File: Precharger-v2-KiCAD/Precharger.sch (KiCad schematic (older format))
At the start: 61 parts, among them J1 Screw_Terminal_01x04, J2 Anderson_PP45_Power_RA, J3 Anderson_PP45_Power_RA, J5 Anderson_PP45_Power_RA, M1 Anderson_PP45_Staple_Nx2, M2 Anderson_PP45_Staple_Nx2, M3 Anderson_PP45_Staple_Nx2, Q1 SQJQ480E, Q2 BSS123, U1 MCP6001-OT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

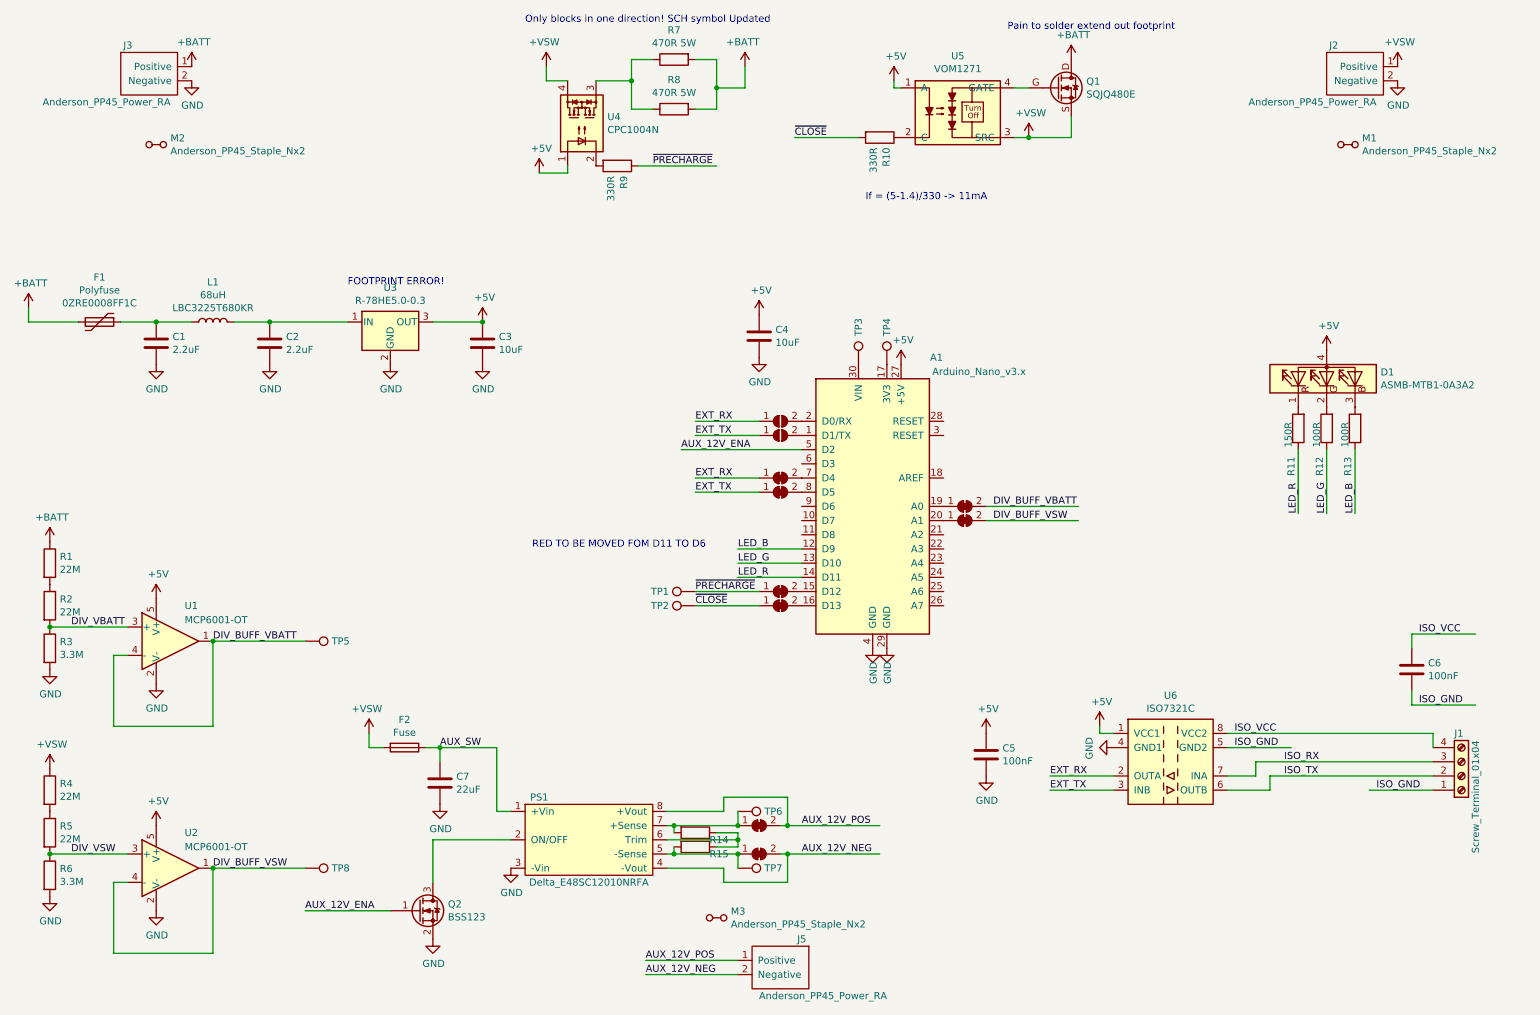
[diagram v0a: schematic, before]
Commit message: Getting a v2 going to try a buck precharge stage
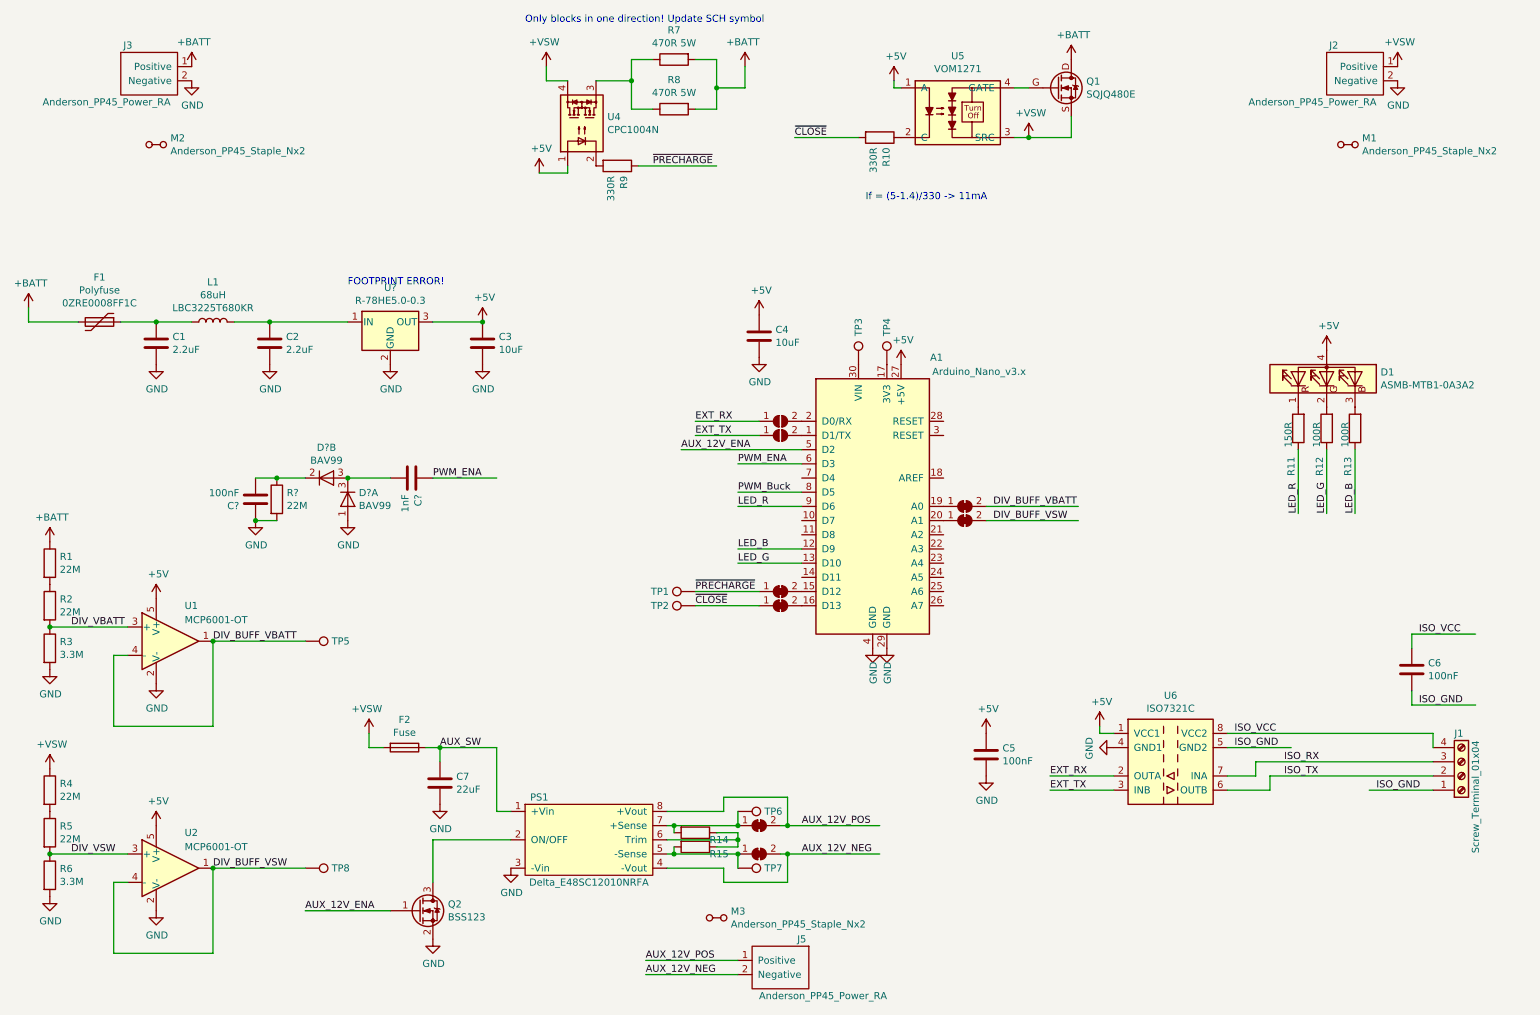
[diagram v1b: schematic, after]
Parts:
- removed JP3, JP4: SolderJumper_2_Bridged, Jumper:SolderJumper-2_P1.3mm_Bridged2Bar_RoundedPad1.0x1.5mm, symbol Jumper:SolderJumper_2_Bridged
- removed U3: R-78HE5.0-0.3, Converter_DCDC:Converter_DCDC_RECOM_R-78HB-0.5_THT, symbol Regulator_Switching:R-78HB5.0-0.5
- added C?: 1nF, Capacitor_SMD:C_0805_2012Metric_Pad1.15x1.40mm_HandSolder, symbol Device:C
- added C?: 100nF, Capacitor_SMD:C_0805_2012Metric_Pad1.15x1.40mm_HandSolder, symbol Device:C
- added D? (x2): BAV99, Package_TO_SOT_SMD:SOT-23, symbol Diode:BAV99
- added R?: 22M, Resistor_SMD:R_0805_2012Metric_Pad1.15x1.40mm_HandSolder, symbol Device:R
- added U?: R-78HE5.0-0.3, General_Library:Converter_DCDC_RECOM_R-78HE-0.3, symbol General_Library:R-78HE5.0-0.3
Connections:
- net labels added: PWM_Buck, PWM_ENA
- wire segments 112 -> 117
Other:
- note added: "Only blocks in one direction! Update SCH symbol"
- note removed: "Only blocks in one direction! SCH symbol Updated"
- note removed: "Pain to solder extend out footprint"
- note removed: "RED TO BE MOVED FOM D11 TO D6"
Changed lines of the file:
@@
-$EndComp
-$Comp
-L Regulator_Switching:R-78HB5.0-0.5 U3
-U 1 1 5DE55D69
-P 3400 2950
-F 0 "U3" H 3400 3192 50  0000 C CNN
-F 1 "R-78HE5.0-0.3" H 3400 3101 50  0000 C CNN
-F 2 "Converter_DCDC:Converter_DCDC_RECOM_R-78HB-0.5_THT" H 3450 2700 50  0001 L CIN
-F 3 "https://www.recom-power.com/pdf/Innoline/R-78HBxx-0.5_L.pdf" H 3400 2950 50  0001 C CNN
-	1    3400 2950
-	1    0    0    -1
 $EndComp
 $Comp
@@
 	1    0    0    -1
 $EndComp
-Text Label 5550 4150 0    50   ~ 0
-EXT_TX
-Text Label 5550 4050 0    50   ~ 0
-EXT_RX
-Wire Wire Line
-	6000 4150 5550 4150
-Wire Wire Line
-	6000 4050 5550 4050
 Text Label 5550 3750 0    50   ~ 0
 EXT_TX
@@
 Wire Wire Line
 	6000 3650 5550 3650
-$Comp
-L Jumper:SolderJumper_2_Bridged JP4
-U 1 1 5DE8F8F2
-P 6150 4150
-F 0 "JP4" H 6150 4263 50  0001 C CNN
-F 1 "SolderJumper_2_Bridged" H 6150 4264 50  0001 C CNN
-F 2 "Jumper:SolderJumper-2_P1.3mm_Bridged2Bar_RoundedPad1.0x1.5mm" H 6150 4150 50  0001 C CNN
-F 3 "~" H 6150 4150 50  0001 C CNN
-	1    6150 4150
-	1    0    0    -1
-$EndComp
 $Comp
 L power:GND #PWR0129
@@
 Wire Wire Line
 	6300 4550 5850 4550
+Text Label 5850 4250 0    50   ~ 0
+LED_R
 Wire Wire Line
 	6300 4650 5850 4650
 Text Label 5850 4650 0    50   ~ 0
 LED_G
+Wire Wire Line
+	6300 4250 5850 4250
 Text Label 5850 4550 0    50   ~ 0
 LED_B
@@
 FOOTPRINT ERROR!
 Text Notes 4350 850  0    50   ~ 0
-Only blocks in one direction! SCH symbol Updated
-Text Notes 7750 900  0    50   ~ 0
-Pain to solder extend out footprint
-$Comp
-L Jumper:SolderJumper_2_Bridged JP3
-U 1 1 5DE8EB88
-P 6150 4050
-F 0 "JP3" H 6150 4163 50  0001 C CNN
-F 1 "SolderJumper_2_Bridged" H 6150 4164 50  0001 C CNN
-F 2 "Jumper:SolderJumper-2_P1.3mm_Bridged2Bar_RoundedPad1.0x1.5mm" H 6150 4050 50  0001 C CNN
-F 3 "~" H 6150 4050 50  0001 C CNN
-	1    6150 4050
-	1    0    0    -1
-$EndComp
-Text Notes 4400 4550 0    50   ~ 0
-RED TO BE MOVED FOM D11 TO D6
-Wire Wire Line
-	6300 4750 5850 4750
-Text Label 5850 4750 0    50   ~ 0
-LED_R
+Only blocks in one direction! Update SCH symbol
+Text Label 5850 3950 0    50   ~ 0
+PWM_ENA
+Wire Wire Line
+	6300 3950 5850 3950
+Text Label 5850 4150 0    50   ~ 0
+PWM_Buck
+Wire Wire Line
+	6300 4150 5850 4150
+$Comp
+L Diode:BAV99 D?
+U 1 1 5E066B6B
+P 3100 4200
+F 0 "D?" V 3054 4278 50  0000 L CNN
+F 1 "BAV99" V 3145 4278 50  0000 L CNN
+F 2 "Package_TO_SOT_SMD:SOT-23" H 3100 4050 50  0001 C CNN
+F 3 "https://assets.nexperia.com/documents/data-sheet/BAV99_SER.pdf" H 3100 4300 50  0001 C CNN
+	1    3100 4200
+	0    1    1    0
+$EndComp
+$Comp
+L Diode:BAV99 D?
+U 2 1 5E068523
+P 2950 4050
+F 0 "D?" H 2950 4265 50  0000 C CNN
+F 1 "BAV99" H 2950 4174 50  0000 C CNN
+F 2 "Package_TO_SOT_SMD:SOT-23" H 2950 3900 50  0001 C CNN
+F 3 "https://assets.nexperia.com/documents/data-sheet/BAV99_SER.pdf" H 2950 4150 50  0001 C CNN
+	2    2950 4050
+	1    0    0    -1
+$EndComp
+$Comp
+L Device:C C?
+U 1 1 5E06EAA7
+P 3550 4050
+F 0 "C?" H 3665 4096 50  0000 L CNN
+F 1 "1nF" H 3665 4005 50  0000 L CNN
+F 2 "Capacitor_SMD:C_0805_2012Metric_Pad1.15x1.40mm_HandSolder" H 3588 3900 50  0001 C CNN
+F 3 "~" H 3550 4050 50  0001 C CNN
+	1    3550 4050
+	0    1    1    0
+$EndComp
+$Comp
+L power:GND #PWR?
+U 1 1 5E07408A
+P 3100 4350
+F 0 "#PWR?" H 3100 4100 50  0001 C CNN
+F 1 "GND" H 3105 4177 50  0000 C CNN
+F 2 "" H 3100 4350 50  0001 C CNN
+F 3 "" H 3100 4350 50  0001 C CNN
+	1    3100 4350
+	1    0    0    -1
+$EndComp
+$Comp
+L Device:C C?
+U 1 1 5E077AE9
+P 2450 4200
+F 0 "C?" H 2565 4246 50  0000 L CNN
+F 1 "100nF" H 2565 4155 50  0000 L CNN
+F 2 "Capacitor_SMD:C_0805_2012Metric_Pad1.15x1.40mm_HandSolder" H 2488 4050 50  0001 C CNN
+F 3 "~" H 2450 4200 50  0001 C CNN
+	1    2450 4200
+	-1   0    0    1
+$EndComp
+$Comp
+L Device:R R?
+U 1 1 5E0796D6
+P 2600 4200
+F 0 "R?" H 2670 4246 50  0000 L CNN
+F 1 "22M" H 2670 4155 50  0000 L CNN
+F 2 "Resistor_SMD:R_0805_2012Metric_Pad1.15x1.40mm_HandSolder" V 2530 4200 50  0001 C CNN
+F 3 "~" H 2600 4200 50  0001 C CNN
+	1    2600 4200
+	1    0    0    -1
+$EndComp
+Wire Wire Line
+	2450 4050 2600 4050
+Connection ~ 2600 4050
+Wire Wire Line
+	2600 4050 2800 4050
+Wire Wire Line
+	3100 4050 3400 4050
+Connection ~ 3100 4050
+$Comp
+L power:GND #PWR?
+U 1 1 5E08DC31
+P 2450 4350
+F 0 "#PWR?" H 2450 4100 50  0001 C CNN
+F 1 "GND" H 2455 4177 50  0000 C CNN
+F 2 "" H 2450 4350 50  0001 C CNN
+F 3 "" H 2450 4350 50  0001 C CNN
+	1    2450 4350
+	1    0    0    -1
+$EndComp
+Wire Wire Line
+	2450 4350 2600 4350
+Connection ~ 2450 4350
+Text Label 3700 4050 0    50   ~ 0
+PWM_ENA
+Wire Wire Line
+	4150 4050 3700 4050
+$Comp
+L General_Library:R-78HE5.0-0.3 U?
+U 1 1 5E0AE6E7
+P 3400 2950
+F 0 "U?" H 3400 3192 50  0000 C CNN
+F 1 "R-78HE5.0-0.3" H 3400 3101 50  0000 C CNN
+F 2 "General_Library:Converter_DCDC_RECOM_R-78HE-0.3" H 3450 2700 50  0001 L CIN
+F 3 "https://recom-power.com/pdf/Innoline/R-78HE-0.3.pdf" H 3400 2950 50  0001 C CNN
+	1    3400 2950
+	1    0    0    -1
+$EndComp
 $EndSCHEMATC

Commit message: Converted v2 to multi sheet schematics
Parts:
- removed C1, C2: 2.2uF, Capacitor_SMD:C_1210_3225Metric_Pad1.42x2.65mm_HandSolder, symbol Device:C
- removed C3: 10uF, Capacitor_SMD:C_0805_2012Metric_Pad1.15x1.40mm_HandSolder, symbol Device:C
- removed C5, C6: 100nF, Capacitor_SMD:C_0805_2012Metric_Pad1.15x1.40mm_HandSolder, symbol Device:C
- removed C7: 22uF, Capacitor_THT:CP_Radial_D10.0mm_P5.00mm, symbol Device:C
- removed F1: Polyfuse, Fuse:Fuse_BelFuse_0ZRE0008FF_L8.3mm_W3.8mm, symbol Device:Polyfuse
- removed F2: Fuse, General_Library:Fuseholder_Clip-5x20mm_Schurter_0751_0052_Horizontal_Open, symbol Device:Fuse
- removed J1: Screw_Terminal_01x04, TerminalBlock_Phoenix:TerminalBlock_Phoenix_PT-1,5-4-3.5-H_1x04_P3.50mm_Horizontal, symbol Connector:Screw_Terminal_01x04
- removed J2, J3, J5: Anderson_PP45_Power_RA, Anderson_Powerpole:Anderson_Powerpole-45A-RA-Bottom-Pair, symbol Anderson_Powerpole:Anderson_PP45_Power_RA
- removed JP10, JP9: SolderJumper_2_Bridged, Jumper:SolderJumper-2_P1.3mm_Bridged2Bar_RoundedPad1.0x1.5mm, symbol Jumper:SolderJumper_2_Bridged
- removed L1: 68uH, Inductor_SMD:L_1210_3225Metric_Pad1.42x2.65mm_HandSolder, symbol Device:L
- removed M1, M2, M3: Anderson_PP45_Staple_Nx2, Anderson_Powerpole:Anderson_Powerpole-staple-Nx2, symbol Anderson_Powerpole:Anderson_PP45_Staple_Nx2
- removed PS1: Delta_E48SC12010NRFA, General_Library:Converter_DCDC_Delta_E48SC12010_THT, symbol General_Library:Delta_E48SC12010NRFA
- removed Q1: SQJQ480E, Precharger:Vishay_PowerPAK_8x8L_Single, symbol Precharger_Lib:SQJQ480E
- removed Q2: BSS123, Package_TO_SOT_SMD:SOT-23, symbol Transistor_FET:BSS123
- removed R1, R2, R4, R5: 22M, Resistor_SMD:R_0805_2012Metric_Pad1.15x1.40mm_HandSolder, symbol Device:R
- removed R10, R9: 330R, Resistor_SMD:R_0805_2012Metric_Pad1.15x1.40mm_HandSolder, symbol Device:R
- removed R14, R15: TRIM_UP, Resistor_SMD:R_0805_2012Metric_Pad1.15x1.40mm_HandSolder, symbol Device:R
- removed R3, R6: 3.3M, Resistor_SMD:R_0805_2012Metric_Pad1.15x1.40mm_HandSolder, symbol Device:R
- removed R7, R8: 470R 5W, Resistor_THT:R_Axial_Power_L25.0mm_W9.0mm_P30.48mm, symbol Device:R
- removed TP5, TP6, TP7, TP8: TestPoint, TestPoint:TestPoint_Keystone_5010-5014_Multipurpose, symbol Connector:TestPoint
- removed U1, U2: MCP6001-OT, Package_TO_SOT_SMD:SOT-23-5_HandSoldering, symbol Amplifier_Operational:MCP6001-OT
- removed U4: CPC1004N, Precharger:SOP-4_3.8x4.1mm_P2.54mm_CPC1004N, symbol Precharger_Lib:CPC1004N
- removed U5: VOM1271, Precharger:SOP-4_4.57x4.92mm_P2.54mm_VOM1271, symbol Precharger_Lib:VOM1271
- removed U6: ISO7321C, Package_SO:SOIC-8_3.9x4.9mm_P1.27mm, symbol Isolator:ISO7321C
- removed U?: R-78HE5.0-0.3, General_Library:Converter_DCDC_RECOM_R-78HE-0.3, symbol General_Library:R-78HE5.0-0.3
- added F?: Fuse, General_Library:Fuseholder_Clip-5x20mm_Schurter_0751_0052_Horizontal_Open, symbol Device:Fuse
- added R?: 10k, Resistor_SMD:R_0805_2012Metric_Pad1.15x1.40mm_HandSolder, symbol Device:R
- added U?: 74LVC1G14, symbol 74xGxx:74LVC1G14
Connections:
- net labels added: Vin, ~ENABLE
- net labels removed: +BATT, AUX_12V_NEG, AUX_12V_POS, AUX_SW, DIV_VBATT, DIV_VSW, ISO_GND, ISO_RX, ISO_TX, ISO_VCC
- wire segments 117 -> 25
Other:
- note removed: "FOOTPRINT ERROR!"
- note removed: "If = (5-1.4)/330 -> 11mA"
- note removed: "Only blocks in one direction! Update SCH symbol"
- moved on the sheet: C?, D?A, D?B, R?

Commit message: Starting update with negative switching
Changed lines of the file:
@@
 S 750  2900 700  600
 U 5E04D7BE
-F0 "5V_Supply" 50
-F1 "5V_Supply.sch" 50
+F0 "Power_Supply" 50
+F1 "Power_Supply.sch" 50
 $EndSheet
 $Sheet
